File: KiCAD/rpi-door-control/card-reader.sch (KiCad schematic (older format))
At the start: 7 parts, among them J2 RJ45, P5 CONN_4, U2 BUZZER

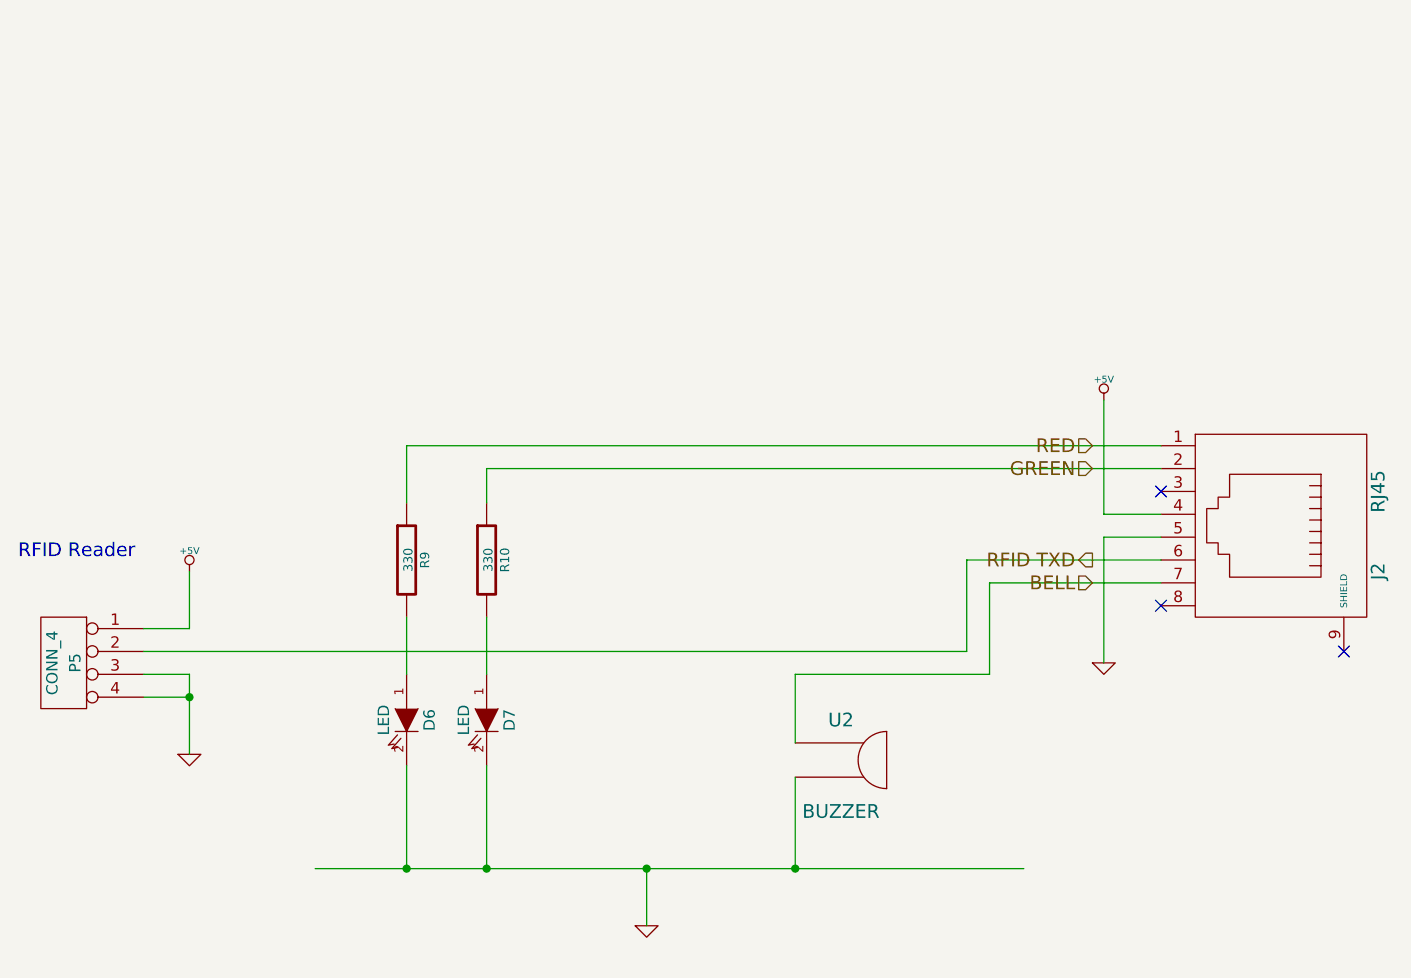
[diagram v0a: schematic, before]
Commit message: Changed cardreader schematic to allow for converting from rj45 to a 6 pin connector of some sort.  Makes things easier for the cardreader board.
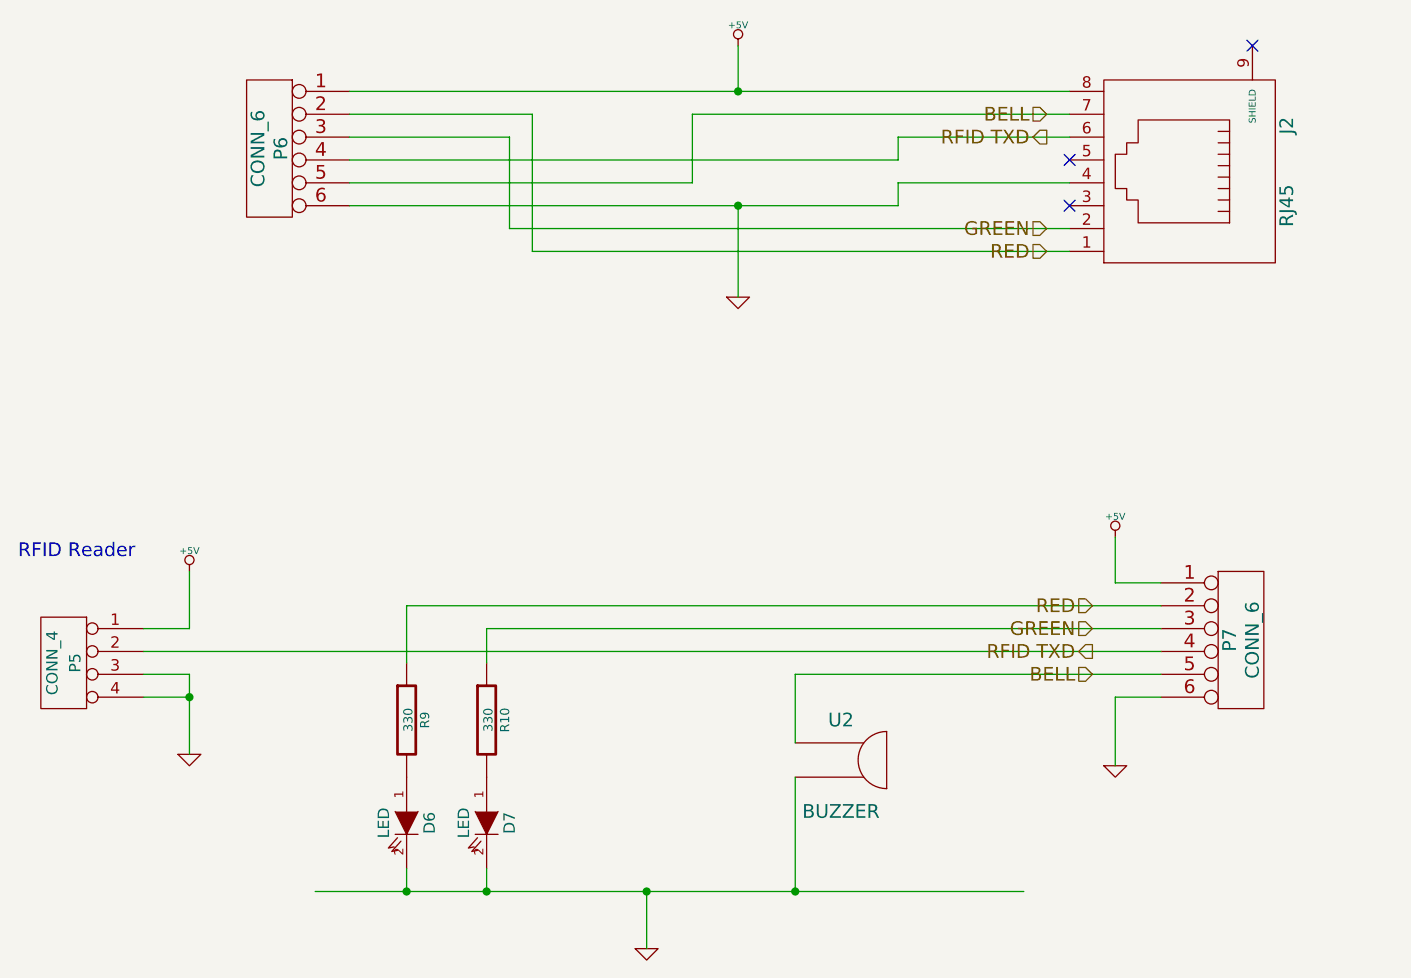
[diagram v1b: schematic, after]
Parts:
- added P6, P7: CONN_6, symbol CONN_6
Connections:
- wire segments 27 -> 39
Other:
- moved on the sheet: D6, D7, R10, R9

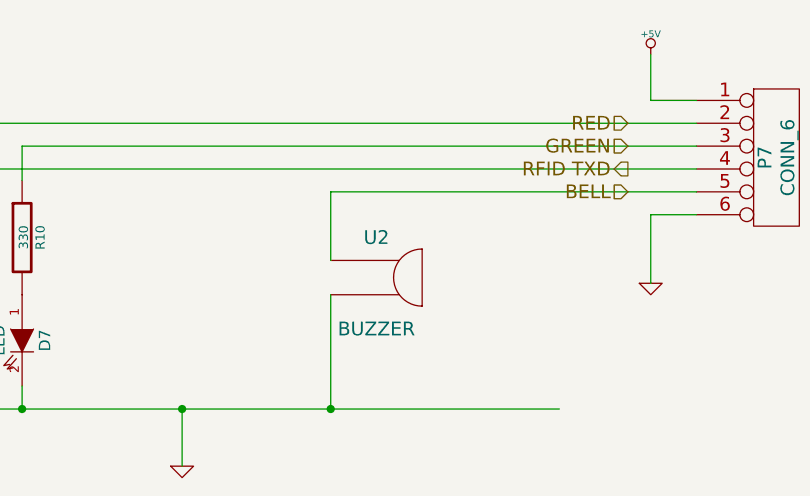
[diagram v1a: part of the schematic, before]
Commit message: cardreader board almost done, just need stupid buzzer to get connected in ratsnest
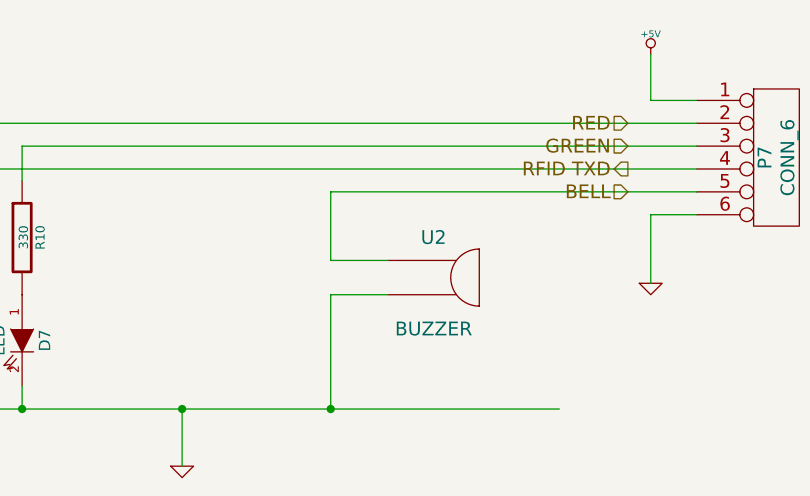
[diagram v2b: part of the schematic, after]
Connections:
- wire segments 39 -> 41
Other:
- moved on the sheet: U2
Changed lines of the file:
@@
 L BUZZER U2
 U 1 1 532A1C21
-P 6150 4400
-F 0 "U2" H 6150 4400 60  0000 C CNN
-F 1 "BUZZER" H 6150 4000 60  0000 C CNN
-F 2 "" H 6150 4400 60  0000 C CNN
-F 3 "" H 6150 4400 60  0000 C CNN
-	1    6150 4400
+P 6400 4400
+F 0 "U2" H 6400 4400 60  0000 C CNN
+F 1 "BUZZER" H 6400 4000 60  0000 C CNN
+F 2 "" H 6400 4400 60  0000 C CNN
+F 3 "" H 6400 4400 60  0000 C CNN
+	1    6400 4400
 	1    0    0    -1
 $EndComp
@@
 Wire Wire Line
 	4600 4000 4600 4150
+Wire Wire Line
+	5950 4500 6200 4500
+Wire Wire Line
+	5950 4650 6200 4650
 $EndSCHEMATC
